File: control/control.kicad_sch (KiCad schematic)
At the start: 35 parts, among them J1 AVR-ISP-6, J2 Conn_01x07_Pin, J3 Conn_01x02_Pin, J4 Conn_01x04_Socket, P1 Conn_01x03_Pin, P2 Conn_01x03_Pin, P3 Conn_01x03_Pin, P4 Conn_01x03_Pin, SW1 SW_Push, U2 ATmega328P-A, Y1 16MHz

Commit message: Revised hardware
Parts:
- removed C10: 100nF, Capacitor_SMD:C_0805_2012Metric, symbol Device:C
- removed C11: 10nF, Capacitor_SMD:C_0805_2012Metric, symbol Device:C
- removed C4: 0.1uF, Capacitor_SMD:C_0805_2012Metric, symbol Device:C
- removed J1: AVR-ISP-6, Connector_PinHeader_2.54mm:PinHeader_2x03_P2.54mm_Vertical_SMD, symbol Connector:AVR-ISP-6
- removed J4: Conn_01x04_Socket, Connector_JST:JST_XH_B4B-XH-A_1x04_P2.50mm_Vertical, symbol Connector:Conn_01x04_Socket
- removed U2: ATmega328P-A, Package_QFP:TQFP-32_7x7mm_P0.8mm, symbol MCU_Microchip_ATmega:ATmega328P-A
- added Battery2: Conn_01x02_Socket, Connector_Wire:SolderWire-2sqmm_1x02_P7.8mm_D2mm_OD3.9mm, symbol Connector:Conn_01x02_Socket
- added C1, C2, C3: 22uF, Capacitor_SMD:C_0805_2012Metric, symbol Device:C
- added C16, C17, C18, C19: 100n, Capacitor_SMD:C_0603_1608Metric, symbol Device:C
- added C7: 0.1uF, Capacitor_SMD:C_0805_2012Metric, symbol Device:C
- added I2C1: FS2, Connector_JST:JST_XH_B4B-XH-A_1x04_P2.50mm_Vertical, symbol Connector:Conn_01x04_Socket
- added I2C2: FS1, Connector_JST:JST_XH_B4B-XH-A_1x04_P2.50mm_Vertical, symbol Connector:Conn_01x04_Socket
- added ISC3: MAIN, Connector_JST:JST_XH_B5B-XH-A_1x05_P2.50mm_Vertical, symbol Connector:Conn_01x05_Socket
- added J1: Conn_01x02_Pin, Connector_JST:JST_XH_B2B-XH-A_1x02_P2.50mm_Vertical, symbol Connector:Conn_01x02_Pin
- added J9: Conn_01x04_Male, Connector_PinHeader_2.54mm:PinHeader_1x04_P2.54mm_Horizontal, symbol Connector:Conn_01x04_Male
- added JP1: Jumper_3_Open, Jumper:SolderJumper-3_P2.0mm_Open_TrianglePad1.0x1.5mm, symbol Jumper:Jumper_3_Open
- added L1: 3.3uH, Inductor_SMD:L_Taiyo-Yuden_NR-60xx, symbol Device:L
- added R19, R2, R20, R3: 10k, Resistor_SMD:R_0603_1608Metric, symbol Device:R_US
- added S5: Conn_01x03_Pin, Connector_JST:JST_EH_B3B-EH-A_1x03_P2.50mm_Vertical, symbol Connector:Conn_01x03_Pin
- added U1: ~, Package_TO_SOT_SMD:TSOT-23-6, symbol Regulators:TPS563208DDCR
- added U1: STM32F103C8Tx, Package_QFP:LQFP-48_7x7mm_P0.5mm, symbol MCU_ST_STM32F1:STM32F103C8Tx
- C8: value 1uF -> 22uF
- C9: value 100nF -> 22uF
- R1: value 10k -> 33.2k
- SW1: footprint Button_Switch_SMD:SW_SPST_SKQG_WithoutStem -> Button_Switch_SMD:SW_SPST_B3U-1000P-B
- Y1: value 16MHz -> 8Mhz
- renumbered J2 to J4, LED1 to LED9, R2 to R5
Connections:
- net +5V: now also I2C1.2 (Pin_2), I2C2.2 (Pin_2), ISC3.2 (Pin_2); no longer C8.1, C9.1, P1.1 (Pin_1), P2.1 (Pin_1), P3.1 (Pin_1), P4.1 (Pin_1), R1.2
- net +BATT: now also Battery2.2 (Pin_2), C1.1, C2.1, C3.1, R3.2, S5.1 (Pin_1), U1.3 (VIN)
- net BUZ: now also U1.19 (PB1)
- net GND: now also C8.1, C9.1, SW1.1, Battery2.1 (Pin_1), C1.2, C16.1, C17.1, C18.1, C19.2, C2.2, C3.2, I2C1.1 (Pin_1), I2C2.1 (Pin_1), ISC3.1 (Pin_1), J1.1 (Pin_1), J9.4 (Pin_4), JP1.1 (A), R19.1, R2.1, S5.3 (Pin_3), U1.1 (GND), U1.20 (PB2), U1.23 (VSS), U1.35 (VSS), U1.47 (VSS), U1.8 (VSSA); no longer C8.2, C9.2, SW1.2
- net LED_{FIELD1}: now also U1.15 (PA5)
- net LED_{FIELD2}: now also U1.16 (PA6)
- net LED_{FIELD3}: now also U1.17 (PA7)
- net LED_{FIELD4}: now also U1.18 (PB0)
- net POT1: now also U1.13 (PA3)
- net POT2: now also U1.12 (PA2)
- net POT3: now also U1.11 (PA1)
- net POT4: now also U1.10 (PA0)
- net SER1: now also U1.25 (PB12)
- net SER2: now also U1.26 (PB13)
- net SER3: now also U1.27 (PB14)
- net SER4: now also U1.28 (PB15)
- net at Y1.1: now also U1.5 (PD0)
- net at Y1.3: now also U1.6 (PD1)
- net RESET renamed +3.3V
- net +3.3V: now also C8.2, C9.2, P1.1 (Pin_1), P2.1 (Pin_1), P3.1 (Pin_1), P4.1 (Pin_1), C16.2, C17.2, C18.2, C19.1, ISC3.5 (Pin_5), J1.2 (Pin_2), J9.1 (Pin_1), JP1.3 (B), L1.1, R20.1, U1.24 (VDD), U1.36 (VDD), U1.48 (VDD), U1.9 (VDDA); no longer SW1.1
- new net: C7.1, L1.2, U1.2 (SW)
- new net: C7.2, U1.6 (VBST)
- new net: R20.2, SW1.2, U1.7 (NRST)
- new net: JP1.2 (C), R19.2, U1.44 (BOOT0)
- new net: R3.1, U1.5 (EN)
- new net: R1.2, R2.2, U1.4 (VFB)
- new net: J9.2 (Pin_2), U1.37 (PA14)
- new net: J9.3 (Pin_3), U1.38 (PA15)
- new net SCL_{TOCTRL}: I2C1.4 (Pin_4), I2C2.4 (Pin_4), U1.21 (PB10)
- new net SCL_{TOMAIN}: ISC3.4 (Pin_4), U1.42 (PB6)
- new net SDA_{TOCTRL}: I2C1.3 (Pin_3), I2C2.3 (Pin_3), U1.22 (PB11)
- new net SDA_{TOMAIN}: ISC3.3 (Pin_3), U1.43 (PB7)
- new net SER5: S5.2 (Pin_2), U1.46 (PB9)
- no-connect marks 4 -> 15
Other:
- note added: "3V3 Voltage Regulator"
- note added: "5V Voltage Regulator"
- note added: "FS1"
- note added: "FS2"
- note added: "TOMAIN"
- note removed: "Bootloader"
- note removed: "Decouplers"
- note removed: "I2C"
- note removed: "Microcontroller"
- note removed: "Reset button"
- note removed: "Voltage Regulator"
- note removed: "iterate on pins"
- note removed: "shorten all dem connectors"
- moved on the sheet: J4

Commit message: added name, title, company, revision # & authors
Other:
- company: (none) -> Human Powered Vehicles Design Team @ UOFT
- title: (none) -> Falcon Control MAIN

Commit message: Touched up values for BOMs
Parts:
- Battery1: now left out of the parts list
- JP1: symbol Jumper:Jumper_3_Open -> Jumper:SolderJumper_3_Open; now left out of the parts list
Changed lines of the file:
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@@
-    (stroke (width 0) (type default))
-  )
-  (wire (pts (xy 113.03 74.93) (xy 113.03 77.47))
     (stroke (width 0) (type default))
   )
@@
     (stroke (width 0) (type default))
   )
+  (wire (pts (xy 113.03 73.66) (xy 113.03 77.47))
+    (stroke (width 0) (type default))
+  )
   (wire (pts (xy 184.15 39.37) (xy 198.12 39.37))
     (stroke (width 0) (type default))
@@
     (stroke (width 0) (type default))
   )
-  (wire (pts (xy 113.03 58.42) (xy 113.03 62.23))
+  (wire (pts (xy 113.03 58.42) (xy 113.03 63.5))
     (stroke (width 0) (type default))
   )
@@
     )
   )
-  (symbol (lib_id "Jumper:Jumper_3_Open") (at 113.03 68.58 90) (unit 1)
-    (in_bom yes) (on_board yes) (dnp no)
+  (symbol (lib_id "Jumper:SolderJumper_3_Open") (at 113.03 68.58 90) (unit 1)
+    (in_bom no) (on_board yes) (dnp no)
     (property "Reference" "JP1" (at 110.49 67.3099 90)
       (effects (font (size 1.27 1.27)) (justify left))
@@
   )
   (symbol (lib_id "Connector:Conn_01x02_Socket") (at 26.67 190.5 180) (unit 1)
-    (in_bom yes) (on_board yes) (dnp no)
+    (in_bom no) (on_board yes) (dnp no)
     (property "Reference" "Battery1" (at 26.67 182.88 0)
       (effects (font (size 1.27 1.27)))

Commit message: changed SWDIO pin from 38 to 34
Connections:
- net at J9.3 (Pin_3): now also U1.34 (PA13); no longer U1.38 (PA15)
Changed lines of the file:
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@@
   (no_connect (at 175.26 80.01))
   (no_connect (at 142.24 105.41))
+  (no_connect (at 175.26 107.95))
   (no_connect (at 142.24 118.11))
   (no_connect (at 142.24 92.71))
-  (no_connect (at 175.26 102.87))
   (no_connect (at 175.26 90.17))
   (no_connect (at 142.24 107.95))
@@
     (stroke (width 0) (type default))
   )
-  (wire (pts (xy 175.26 107.95) (xy 181.61 107.95))
-    (stroke (width 0) (type default))
-  )
   (wire (pts (xy 165.1 57.15) (xy 165.1 64.77))
     (stroke (width 0) (type default))
@@
     (stroke (width 0) (type default))
   )
+  (wire (pts (xy 181.61 107.95) (xy 175.26 102.87))
+    (stroke (width 0) (type default))
+  )

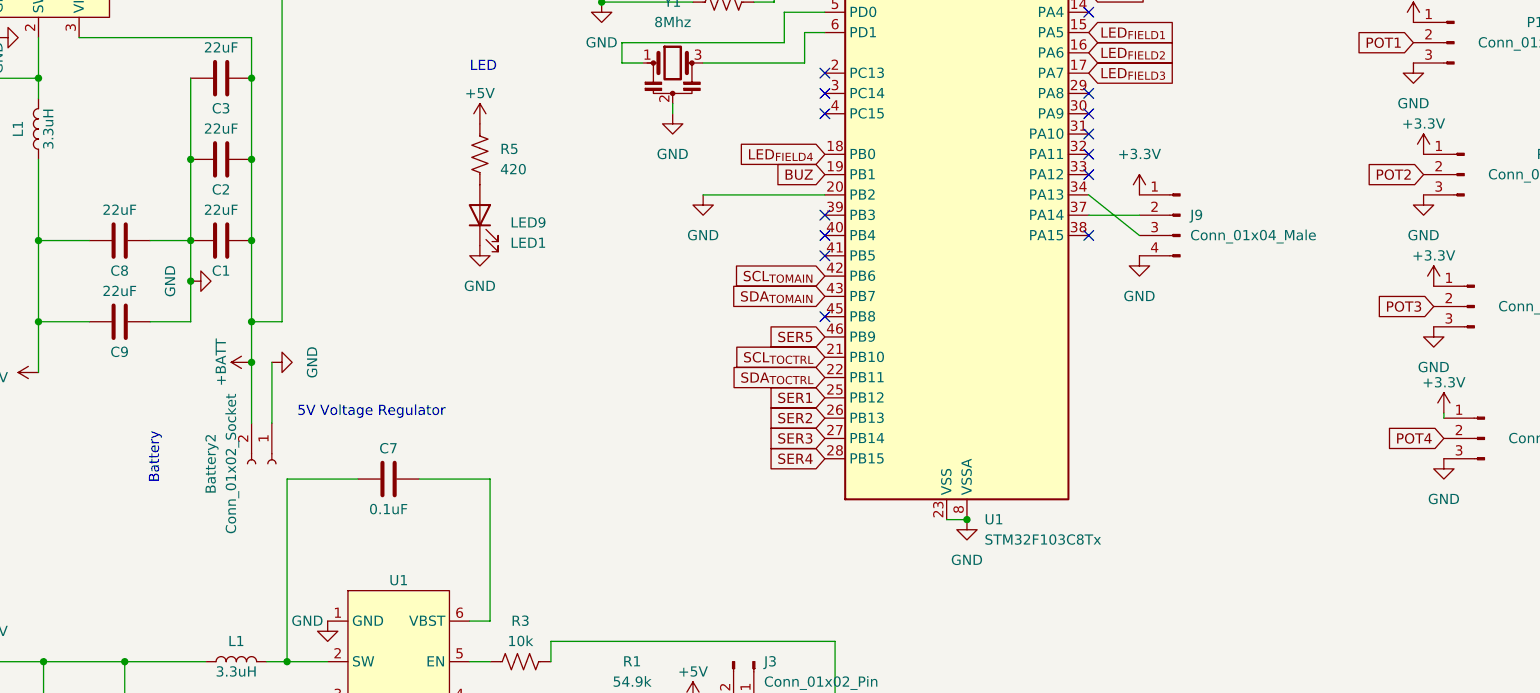
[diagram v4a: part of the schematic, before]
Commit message: Touchups to revised control board
- Removed redundant battery connection in schematic
- Added labels to programming signals in schematic
- Added "Rev. ##" label on board
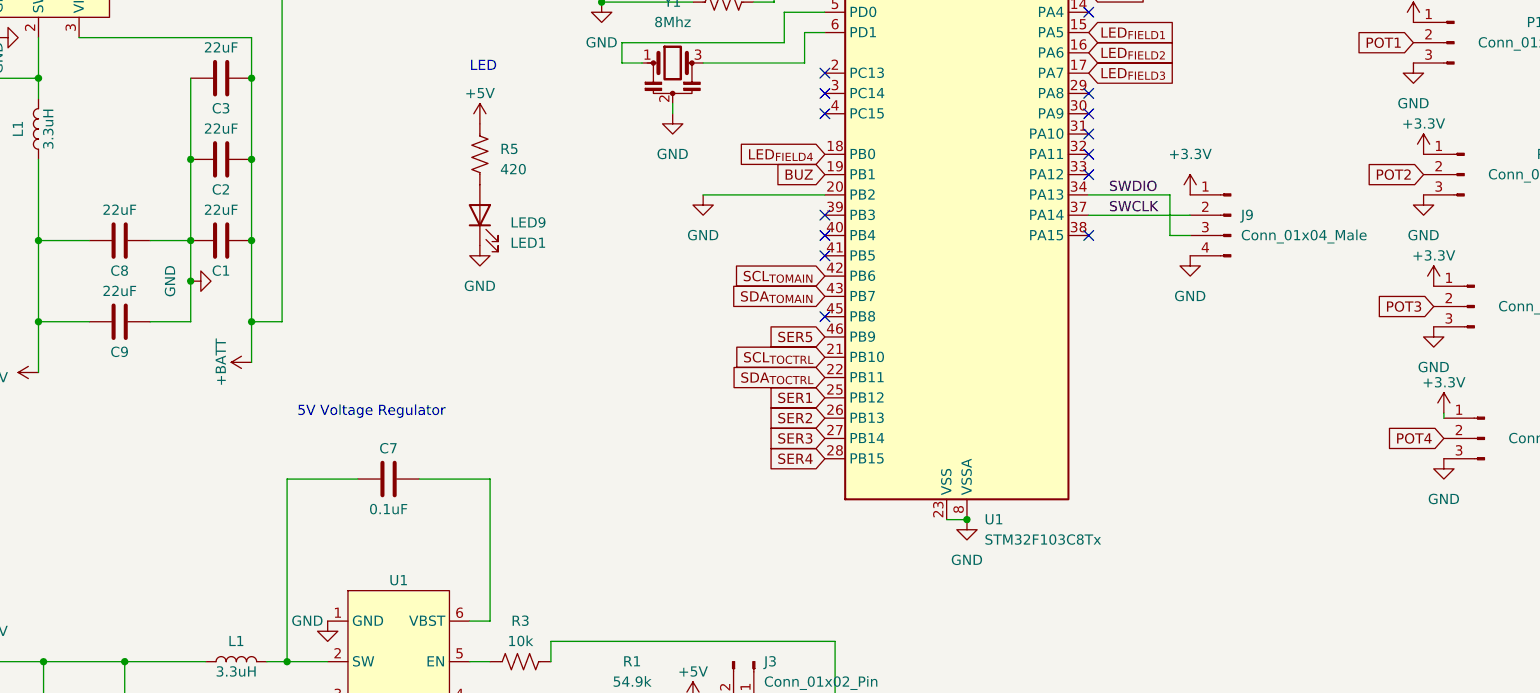
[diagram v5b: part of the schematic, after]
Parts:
- removed Battery2: Conn_01x02_Socket, Connector_Wire:SolderWire-2sqmm_1x02_P7.8mm_D2mm_OD3.9mm, symbol Connector:Conn_01x02_Socket
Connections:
- net SWCLK: now reaches J9.2 (Pin_2), U1.37 (PA14)
- net SWDIO: now reaches J9.3 (Pin_3), U1.34 (PA13)
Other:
- moved on the sheet: J9
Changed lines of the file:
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@@
   (junction (at 62.865 113.665) (diameter 0) (color 0 0 0 0)
   )
-  (junction (at 70.485 123.825) (diameter 0) (color 0 0 0 0)
-  )
   (junction (at 48.895 37.465) (diameter 0) (color 0 0 0 0)
   )
@@
     (stroke (width 0) (type default))
   )
+  (wire (pts (xy 185.42 107.95) (xy 187.96 107.95))
+    (stroke (width 0) (type default))
+  )
   (wire (pts (xy 165.1 34.29) (xy 165.1 44.45))
     (stroke (width 0) (type default))
@@
     (stroke (width 0) (type default))
   )
+  (wire (pts (xy 175.26 102.87) (xy 185.42 102.87))
+    (stroke (width 0) (type default))
+  )
   (wire (pts (xy 72.39 161.29) (xy 74.93 161.29))
     (stroke (width 0) (type default))
@@
     (stroke (width 0) (type default))
   )
-  (wire (pts (xy 181.61 107.95) (xy 175.26 102.87))
-    (stroke (width 0) (type default))
-  )
   (wire (pts (xy 80.01 166.37) (xy 80.01 187.96))
     (stroke (width 0) (type default))
@@
     (stroke (width 0) (type default))
   )
-  (wire (pts (xy 175.26 105.41) (xy 181.61 105.41))
+  (wire (pts (xy 175.26 105.41) (xy 187.96 105.41))
     (stroke (width 0) (type default))
   )
@@
     (stroke (width 0) (type default))
   )
-  (wire (pts (xy 70.485 131.445) (xy 70.485 123.825))
-    (stroke (width 0) (type default))
-  )
   (wire (pts (xy 134.62 52.07) (xy 137.16 52.07))
     (stroke (width 0) (type default))
@@
     (stroke (width 0) (type default))
   )
-  (wire (pts (xy 73.025 123.825) (xy 73.025 131.445))
+  (wire (pts (xy 54.61 161.29) (xy 64.77 161.29))
     (stroke (width 0) (type default))
   )
-  (wire (pts (xy 54.61 161.29) (xy 64.77 161.29))
+  (wire (pts (xy 185.42 102.87) (xy 185.42 107.95))
     (stroke (width 0) (type default))
   )
@@
     (effects (font (size 1.27 1.27)) (justify left bottom))
   )
-  (text "Battery" (at 59.055 139.065 90)
+  (text "Battery" (at 24.13 176.53 0)
     (effects (font (size 1.27 1.27)) (justify left bottom))
   )
-  (text "Battery" (at 24.13 176.53 0)
+  (label "SWDIO" (at 177.8 102.87 0) (fields_autoplaced)
+    (effects (font (size 1.27 1.27)) (justify left bottom))
+  )
+  (label "SWCLK" (at 177.8 105.41 0) (fields_autoplaced)
     (effects (font (size 1.27 1.27)) (justify left bottom))
   )
@@
     )
   )
-  (symbol (lib_id "power:GND") (at 181.61 110.49 0) (unit 1)
+  (symbol (lib_id "power:GND") (at 187.96 110.49 0) (unit 1)
     (in_bom yes) (on_board yes) (dnp no) (fields_autoplaced)
-    (property "Reference" "#PWR037" (at 181.61 116.84 0)
+    (property "Reference" "#PWR037" (at 187.96 116.84 0)
       (effects (font (size 1.27 1.27)) hide)
     )
-    (property "Value" "GND" (at 181.61 115.57 0)
+    (property "Value" "GND" (at 187.96 115.57 0)
       (effects (font (size 1.27 1.27)))
     )
-    (property "Footprint" "" (at 181.61 110.49 0)
+    (property "Footprint" "" (at 187.96 110.49 0)
       (effects (font (size 1.27 1.27)) hide)
     )
-    (property "Datasheet" "" (at 181.61 110.49 0)
+    (property "Datasheet" "" (at 187.96 110.49 0)
       (effects (font (size 1.27 1.27)) hide)
     )
@@
     )
   )
-  (symbol (lib_id "Connector:Conn_01x04_Male") (at 186.69 105.41 0) (mirror y) (unit 1)
+  (symbol (lib_id "Connector:Conn_01x04_Male") (at 193.04 105.41 0) (mirror y) (unit 1)
     (in_bom yes) (on_board yes) (dnp no) (fields_autoplaced)
-    (property "Reference" "J9" (at 187.96 105.4099 0)
+    (property "Reference" "J9" (at 194.31 105.4099 0)
       (effects (font (size 1.27 1.27)) (justify right))
     )
-    (property "Value" "Conn_01x04_Male" (at 187.96 107.9499 0)
+    (property "Value" "Conn_01x04_Male" (at 194.31 107.9499 0)
       (effects (font (size 1.27 1.27)) (justify right))
     )
-    (property "Footprint" "Connector_PinHeader_2.54mm:PinHeader_1x04_P2.54mm_Horizontal" (at 186.69 105.41 0)
+    (property "Footprint" "Connector_PinHeader_2.54mm:PinHeader_1x04_P2.54mm_Horizontal" (at 193.04 105.41 0)
       (effects (font (size 1.27 1.27)) hide)
     )
-    (property "Datasheet" "~" (at 186.69 105.41 0)
+    (property "Datasheet" "~" (at 193.04 105.41 0)
       (effects (font (size 1.27 1.27)) hide)
     )
@@
     )
   )
-  (symbol (lib_id "Connector:Conn_01x02_Socket") (at 73.025 136.525 270) (unit 1)
-    (in_bom yes) (on_board yes) (dnp no)
-    (property "Reference" "Battery2" (at 65.405 136.525 0)
-      (effects (font (size 1.27 1.27)))
-    )
-    (property "Value" "Conn_01x02_Socket" (at 67.945 136.525 0)
-      (effects (font (size 1.27 1.27)))
-    )
-    (property "Footprint" "Connector_Wire:SolderWire-2sqmm_1x02_P7.8mm_D2mm_OD3.9mm" (at 73.025 136.525 0)
-      (effects (font (size 1.27 1.27)) hide)
-    )
-    (property "Datasheet" "~" (at 73.025 136.525 0)
-      (effects (font (size 1.27 1.27)) hide)
-    )
-    (pin "1")
-    (pin "2")
-    (instances
-      (project "control"
-        (path "/e7781990-9217-47e0-bccf-d5b77eec6675"
-          (reference "Battery2") (unit 1)
-        )
-      )
-    )
-  )
   (symbol (lib_id "Device:C") (at 161.29 57.15 270) (mirror x) (unit 1)
     (in_bom yes) (on_board yes) (dnp no)
@@
     )
   )
-  (symbol (lib_id "power:GND") (at 73.025 123.825 90) (mirror x) (unit 1)
-    (in_bom yes) (on_board yes) (dnp no) (fields_autoplaced)
-    (property "Reference" "#PWR044" (at 79.375 123.825 0)
-      (effects (font (size 1.27 1.27)) hide)
-    )
-    (property "Value" "GND" (at 78.105 123.825 0)
-      (effects (font (size 1.27 1.27)))
-    )
-    (property "Footprint" "" (at 73.025 123.825 0)
-      (effects (font (size 1.27 1.27)) hide)
-    )
-    (property "Datasheet" "" (at 73.025 123.825 0)
-      (effects (font (size 1.27 1.27)) hide)
-    )
-    (pin "1")
-    (instances
-      (project "control"
-        (path "/e7781990-9217-47e0-bccf-d5b77eec6675"
-          (reference "#PWR044") (unit 1)
-        )
-      )
-    )
-  )
   (symbol (lib_id "Device:R_US") (at 118.11 166.37 270) (unit 1)
     (in_bom yes) (on_board yes) (dnp no) (fields_autoplaced)
@@
     )
   )
-  (symbol (lib_id "power:+3.3V") (at 181.61 102.87 0) (unit 1)
+  (symbol (lib_id "power:+3.3V") (at 187.96 102.87 0) (unit 1)
     (in_bom yes) (on_board yes) (dnp no) (fields_autoplaced)
-    (property "Reference" "#PWR036" (at 181.61 106.68 0)
+    (property "Reference" "#PWR036" (at 187.96 106.68 0)
       (effects (font (size 1.27 1.27)) hide)
     )
-    (property "Value" "+3.3V" (at 181.61 97.79 0)
+    (property "Value" "+3.3V" (at 187.96 97.79 0)
       (effects (font (size 1.27 1.27)))
     )
-    (property "Footprint" "" (at 181.61 102.87 0)
+    (property "Footprint" "" (at 187.96 102.87 0)
       (effects (font (size 1.27 1.27)) hide)
     )
-    (property "Datasheet" "" (at 181.61 102.87 0)
+    (property "Datasheet" "" (at 187.96 102.87 0)
       (effects (font (size 1.27 1.27)) hide)
     )
